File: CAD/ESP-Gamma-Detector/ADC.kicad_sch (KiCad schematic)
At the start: 1 part, among them U5 ADS8675IPWR

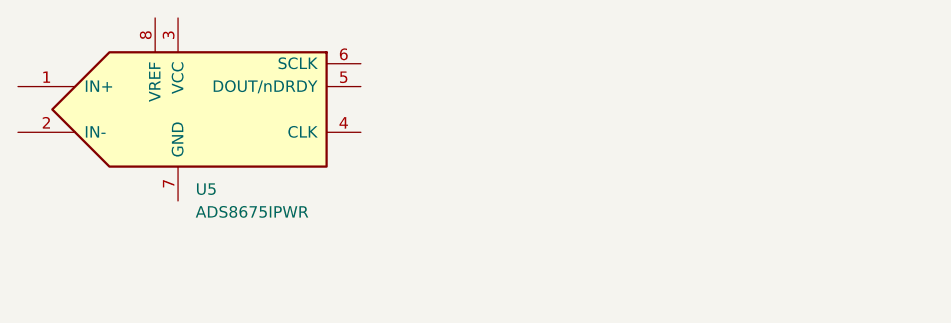
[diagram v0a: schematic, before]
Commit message: Feat: New ADC
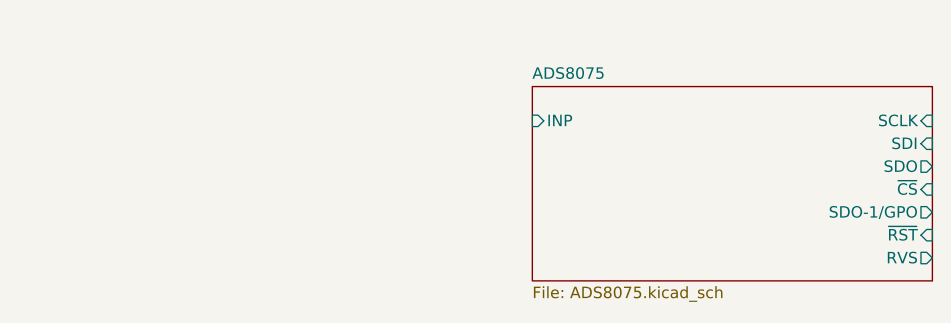
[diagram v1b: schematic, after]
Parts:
- removed U5: ADS8675IPWR, Package_SO:TSSOP-16_4.4x5mm_P0.65mm, symbol adclib:ADS1251
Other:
- added sheet ADS8075 (ADS8075.kicad_sch)
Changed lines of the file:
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@@
 (kicad_sch (version 20230121) (generator eeschema)
   (paper "A4")
-  (symbol (lib_id "adclib:ADS1251") (at 161.29 87.63 0) (unit 1)
-    (in_bom yes) (on_board yes) (dnp no) (fields_autoplaced)
-    (property "Reference" "U5" (at 160.7059 96.52 0)
+  (sheet (at 198.12 85.09) (size 44.45 21.59) (fields_autoplaced)
+    (stroke (width 0.1524) (type solid))
+    (fill (color 0 0 0 0.0000))
+    (property "Sheetname" "ADS8075" (at 198.12 84.3784 0)
+      (effects (font (size 1.27 1.27)) (justify left bottom))
+    )
+    (property "Sheetfile" "ADS8075.kicad_sch" (at 198.12 107.2646 0)
+      (effects (font (size 1.27 1.27)) (justify left top))
+    )
+    (pin "INP" input (at 198.12 88.9 180)
       (effects (font (size 1.27 1.27)) (justify left))
     )
-    (property "Value" "ADS8675IPWR" (at 160.7059 99.06 0)
-      (effects (font (size 1.27 1.27)) (justify left))
+    (pin "~{RST}" input (at 242.57 101.6 0)
+      (effects (font (size 1.27 1.27)) (justify right))
     )
-    (property "Footprint" "Package_SO:TSSOP-16_4.4x5mm_P0.65mm" (at 161.29 100.33 0)
-      (effects (font (size 1.27 1.27) italic) hide)
+    (pin "SDO" output (at 242.57 93.98 0)
+      (effects (font (size 1.27 1.27)) (justify right))
     )
-    (property "Datasheet" "http://www.ti.com/lit/ds/symlink/ads1251.pdf" (at 158.75 87.63 0)
-      (effects (font (size 1.27 1.27)) hide)
+    (pin "SDI" input (at 242.57 91.44 0)
+      (effects (font (size 1.27 1.27)) (justify right))
     )
-    (pin "1")
-    (pin "2")
-    (pin "3")
-    (pin "4")
-    (pin "5")
-    (pin "6")
-    (pin "7")
-    (pin "8")
+    (pin "SCLK" input (at 242.57 88.9 0)
+      (effects (font (size 1.27 1.27)) (justify right))
+    )
+    (pin "~{CS}" input (at 242.57 96.52 0)
+      (effects (font (size 1.27 1.27)) (justify right))
+    )
+    (pin "SDO-1{slash}GPO" output (at 242.57 99.06 0)
+      (effects (font (size 1.27 1.27)) (justify right))
+    )
+    (pin "RVS" output (at 242.57 104.14 0)
+      (effects (font (size 1.27 1.27)) (justify right))
+    )
     (instances
-      (project "aqsense_cheapass"
-        (path "/51bbc301-ea4a-44e0-84a7-cf42c64443ca/47e335a8-3e50-4b71-b8fd-14f2b24805b1"
-          (reference "U5") (unit 1)
-        )
+      (project "ESP-Gamma-Detector"
+        (path "/51bbc301-ea4a-44e0-84a7-cf42c64443ca/47e335a8-3e50-4b71-b8fd-14f2b24805b1" (page "10"))
       )
     )
